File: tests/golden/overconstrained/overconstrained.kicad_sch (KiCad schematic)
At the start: 2 parts, among them J1 CONN_BRK_1X04, J2 CONN_BRK_1X04

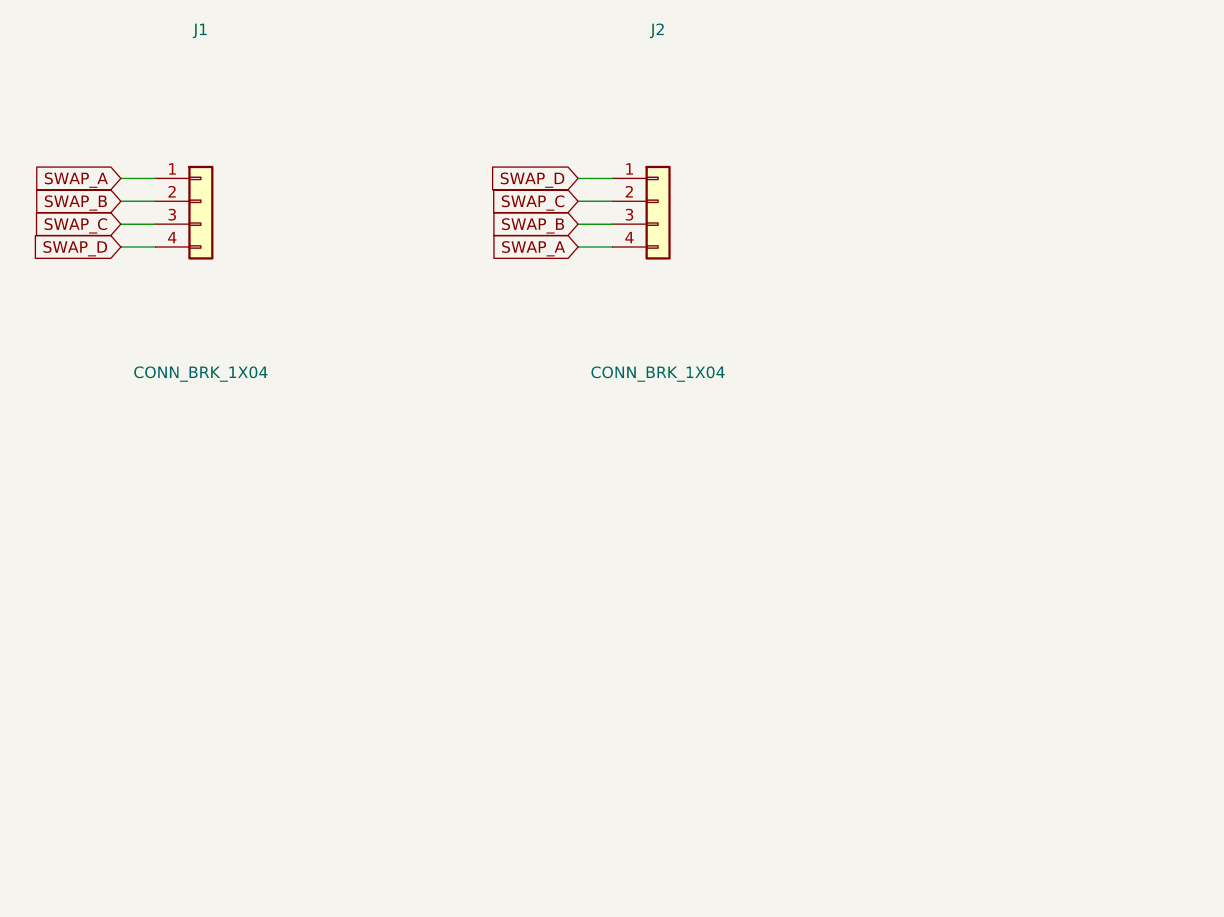
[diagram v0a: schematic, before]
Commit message: M14: the sheet that could not be reviewed, and the router that was never asked
Two themes. The generated schematics were electrically correct and unreadable:
every fact the source knew about *why* a part exists -- `role`, `for:`, the module
hierarchy, the netlist graph -- died at the sheet boundary, and a capacitor whose
purpose is to sit at one pin of one IC was placed by its position in a sorted list.
On pcie-sata that was 157.5 mm from the pin it decouples, on a sheet 594 mm wide.
And manual routing was something that *happened* to a board rather than something
the source could declare.

Placement is now derived in five steps (aipcb/compile/sheet.py): satellites attach
to what they serve, module instances become named clusters, blocks are ranked left
to right by breadth-first distance over signal nets only, ordered by a barycentre
sweep, and placed by measured extents. Rails point up, grounds point down, and a
crowded pin row keeps its labels because a ground symbol is wider than a 2.54 mm
pitch.

Measured across all eleven examples, before -> after:

  overlapping drawn items            71 -> 0
  mean decoupling-to-IC distance     down on every example with a local cap
    pcie-sata                     157.5 -> 27.8 mm
  total wire length                1196 -> 1151 mm
  wire crossings                      0 -> 0   (a stub idiom has none; said so)
  pcie-sata paper                    A1 -> A3

Nothing electrical moved, and it is proved rather than asserted: KiCad's own
netlister run against the pre- and post-M14 sheets agrees net name for net name and
pin for pin on all eleven; ERC is still 0; two builds are byte-identical; and
regenerating the golden tree moved eleven files, all of them .kicad_sch.

Three defects the *measurement* found, not the eye: KiCad's libraries stack a
part's repeated power pins on one coordinate and we drew nine identical GND labels
there; reference and value text was placed from the pin field rather than from the
drawing; and a block a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
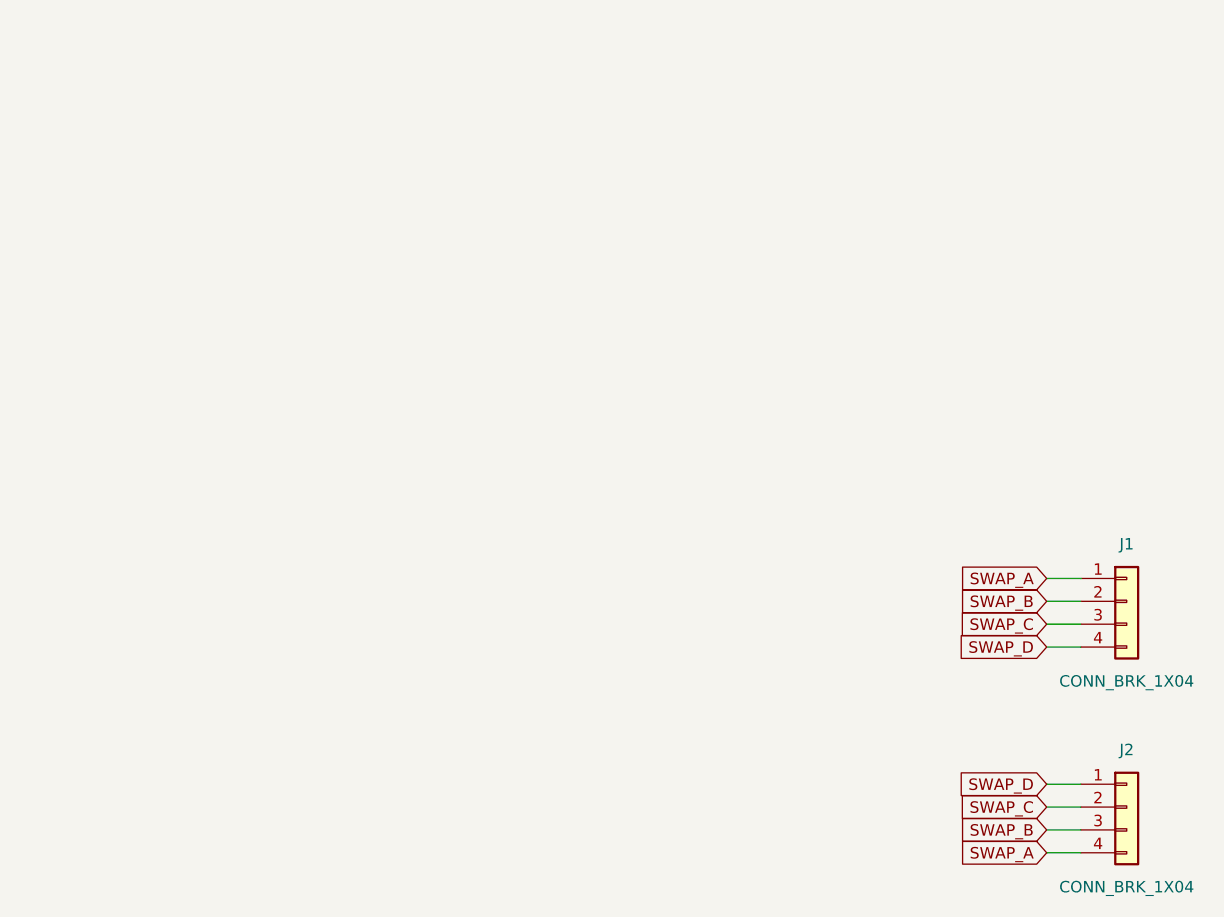
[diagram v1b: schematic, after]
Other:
- moved on the sheet: J1, J2
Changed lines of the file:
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@@
 		(company "")
 		(comment 1 "Two headers wired in reverse with one channel between them and one layer to do it on, so the router hands over what it cannot route legally.")
+		(comment 9 "aipcb-sheet:2a767cf08e094e00")
 	)
 	(symbol
 		(lib_id "Connector_Generic:Conn_01x04")
-		(at 50.8 48.26 0)
+		(at 153.67 92.71 0)
 		(unit 1)
 		(exclude_from_sim no)
@@
 		(dnp no)
 		(property "Reference" "J1"
-			(at 50.8 29.21 0)
+			(at 153.67 86.36 0)
 			(effects
 				(font
@@
 		)
 		(property "Value" "CONN_BRK_1X04"
-			(at 50.8 67.31 0)
+			(at 153.67 101.6 0)
 			(effects
 				(font
@@
 		)
 		(property "Footprint" "Connector_PinHeader_2.54mm:PinHeader_1x04_P2.54mm_Vertical"
-			(at 50.8 48.26 0)
+			(at 153.67 92.71 0)
 			(effects
 				(font
@@
 		)
 		(property "Datasheet" ""
-			(at 50.8 48.26 0)
+			(at 153.67 92.71 0)
 			(effects
 				(font
@@
 		)
 		(property "Description" "4-pin 2.54 mm breakout header"
-			(at 50.8 48.26 0)
+			(at 153.67 92.71 0)
 			(effects
 				(font
@@
 		)
 		(property "aipcb.reason" "The left-hand side of the reversal."
-			(at 50.8 48.26 0)
+			(at 153.67 92.71 0)
 			(effects
 				(font
@@
 		)
 		(property "aipcb.role" "connector"
-			(at 50.8 48.26 0)
+			(at 153.67 92.71 0)
 			(effects
 				(font
@@
 		)
 		(property "aipcb.path" "J1"
-			(at 50.8 48.26 0)
+			(at 153.67 92.71 0)
 			(effects
 				(font
@@
 	(symbol
 		(lib_id "Connector_Generic:Conn_01x04")
-		(at 101.6 48.26 0)
+		(at 153.67 115.57 0)
 		(unit 1)
 		(exclude_from_sim no)
@@
 		(dnp no)
 		(property "Reference" "J2"
-			(at 101.6 29.21 0)
+			(at 153.67 109.22 0)
 			(effects
 				(font
@@
 		)
 		(property "Value" "CONN_BRK_1X04"
-			(at 101.6 67.31 0)
+			(at 153.67 124.46 0)
 			(effects
 				(font
@@
 		)
 		(property "Footprint" "Connector_PinHeader_2.54mm:PinHeader_1x04_P2.54mm_Vertical"
-			(at 101.6 48.26 0)
+			(at 153.67 115.57 0)
 			(effects
 				(font
@@
 		)
 		(property "Datasheet" ""
-			(at 101.6 48.26 0)
+			(at 153.67 115.57 0)
 			(effects
 				(font
@@
 		)
 		(property "Description" "4-pin 2.54 mm breakout header"
-			(at 101.6 48.26 0)
+			(at 153.67 115.57 0)
 			(effects
 				(font
@@
 		)
 		(property "aipcb.reason" "The right-hand side, with its pin order reversed. That is what makes the four connections a permutation no single plane can hold."
-			(at 101.6 48.26 0)
+			(at 153.67 115.57 0)
 			(effects
 				(font
@@
 		)
 		(property "aipcb.role" "connector"
-			(at 101.6 48.26 0)
+			(at 153.67 115.57 0)
 			(effects
 				(font
@@
 		)
 		(property "aipcb.path" "J2"
-			(at 101.6 48.26 0)
+			(at 153.67 115.57 0)
 			(effects
 				(font
@@
 	(wire
 		(pts
-			(xy 45.72 45.72)
-			(xy 41.91 45.72)
+			(xy 148.59 90.17)
+			(xy 144.78 90.17)
 		)
 		(stroke
@@
 	(global_label "SWAP_A"
 		(shape input)
-		(at 41.91 45.72 180)
-		(effects
-			(font
-				(size 1.27 1.27)
-			)
-			(justify right)
-		)
-	)
-	(wire
-		(pts
-			(xy 45.72 48.26)
-			(xy 41.91 48.26)
+		(at 144.78 90.17 180)
+		(effects
+			(font
+				(size 1.27 1.27)
+			)
+			(justify right)
+		)
+	)
+	(wire
+		(pts
+			(xy 148.59 92.71)
+			(xy 144.78 92.71)
 		)
 		(stroke
@@
 	(global_label "SWAP_B"
 		(shape input)
-		(at 41.91 48.26 180)
-		(effects
-			(font
-				(size 1.27 1.27)
-			)
-			(justify right)
-		)
-	)
-	(wire
-		(pts
-			(xy 45.72 50.8)
-			(xy 41.91 50.8)
+		(at 144.78 92.71 180)
+		(effects
+			(font
+				(size 1.27 1.27)
+			)
+			(justify right)
+		)
+	)
+	(wire
+		(pts
+			(xy 148.59 95.25)
+			(xy 144.78 95.25)
 		)
 		(stroke
@@
 	(global_label "SWAP_C"
 		(shape input)
-		(at 41.91 50.8 180)
-		(effects
-			(font
-				(size 1.27 1.27)
-			)
-			(justify right)
-		)
-	)
-	(wire
-		(pts
-			(xy 45.72 53.34)
-			(xy 41.91 53.34)
+		(at 144.78 95.25 180)
+		(effects
+			(font
+				(size 1.27 1.27)
+			)
+			(justify right)
+		)
+	)
+	(wire
+		(pts
+			(xy 148.59 97.79)
+			(xy 144.78 97.79)
 		)
 		(stroke
@@
 	(global_label "SWAP_D"
 		(shape input)
-		(at 41.91 53.34 180)
-		(effects
-			(font
-				(size 1.27 1.27)
-			)
-			(justify right)
-		)
-	)
-	(wire
-		(pts
-			(xy 96.52 45.72)
-			(xy 92.71 45.72)
+		(at 144.78 97.79 180)
+		(effects
+			(font
+				(size 1.27 1.27)
+			)
+			(justify right)
+		)
+	)
+	(wire
+		(pts
+			(xy 148.59 113.03)
+			(xy 144.78 113.03)
 		)
 		(stroke
@@
 	(global_label "SWAP_D"
 		(shape input)
-		(at 92.71 45.72 180)
-		(effects
-			(font
-				(size 1.27 1.27)
-			)
-			(justify right)
-		)
-	)
-	(wire
-		(pts
-			(xy 96.52 48.26)
-			(xy 92.71 48.26)
+		(at 144.78 113.03 180)
+		(effects
+			(font
+				(size 1.27 1.27)
+			)
+			(justify right)
+		)
+	)
+	(wire
+		(pts
+			(xy 148.59 115.57)
+			(xy 144.78 115.57)
 		)
 		(stroke
@@
 	(global_label "SWAP_C"
 		(shape input)
-		(at 92.71 48.26 180)
-		(effects
-			(font
-				(size 1.27 1.27)
-			)
-			(justify right)
-		)
-	)
-	(wire
-		(pts
-			(xy 96.52 50.8)
-			(xy 92.71 50.8)
+		(at 144.78 115.57 180)
+		(effects
+			(font
+				(size 1.27 1.27)
+			)
+			(justify right)
+		)
+	)
+	(wire
+		(pts
+			(xy 148.59 118.11)
+			(xy 144.78 118.11)
 		)
 		(stroke
@@
 	(global_label "SWAP_B"
 		(shape input)
-		(at 92.71 50.8 180)
-		(effects
-			(font
-				(size 1.27 1.27)
-			)
-			(justify right)
-		)
-	)
-	(wire
-		(pts
-			(xy 96.52 53.34)
-			(xy 92.71 53.34)
+		(at 144.78 118.11 180)
+		(effects
+			(font
+				(size 1.27 1.27)
+			)
+			(justify right)
+		)
+	)
+	(wire
+		(pts
+			(xy 148.59 120.65)
+			(xy 144.78 120.65)
 		)
 		(stroke
@@
 	(global_label "SWAP_A"
 		(shape input)
-		(at 92.71 53.34 180)
-		(effects
-			(font
+		(at 144.78 120.65 180)
+		(effects
+			(font
